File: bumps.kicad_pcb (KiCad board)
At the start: 2 copper layers, 111.1 x 65.4 mm, 126 parts, among them M1 CONN_1, M2 CONN_1, M3 CONN_1, P1 Micro-E, P10 Mot-A, P11 Mot-A, P12 Mot-X, P13 T1, P14 T2, P15 T3, P16 MPower, P17 PWM-2, P18 PWM-1, P19 END-X, P2 DIL6, P20 END-Y, P21 END-Z, P22 Mot-X, P23 Mot-Y, P24 Mot-Y, P25 Mot-Z, P26 Mot-Z, P27 Aux, P29 PWM, P3 Mot-E, P4 Mot-E, P5 DIL6, P6 DIL6, P7 DIL6, P8 P8 Header, P9 P9 Header, Q1 N-FET, Q2 N-FET, Q3 FDS9926A, Q4 FDS9926A, U1 E-Polo, U2 A-Polo, U3 X-Polo, U4 Y-Polo, U5 Z-Polo, U6 MC34063, U7 AP1117/3.3

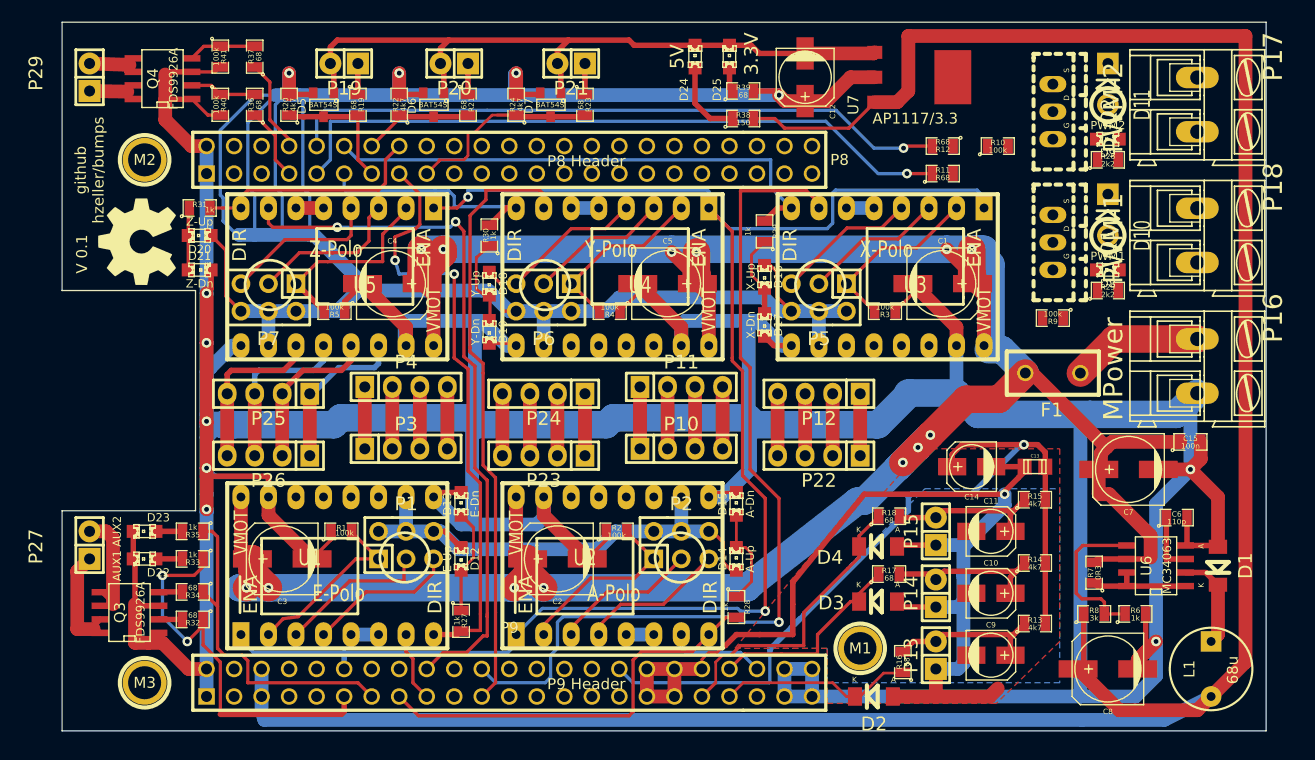
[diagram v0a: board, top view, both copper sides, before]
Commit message: o Solve 3.3V connect between two areas.
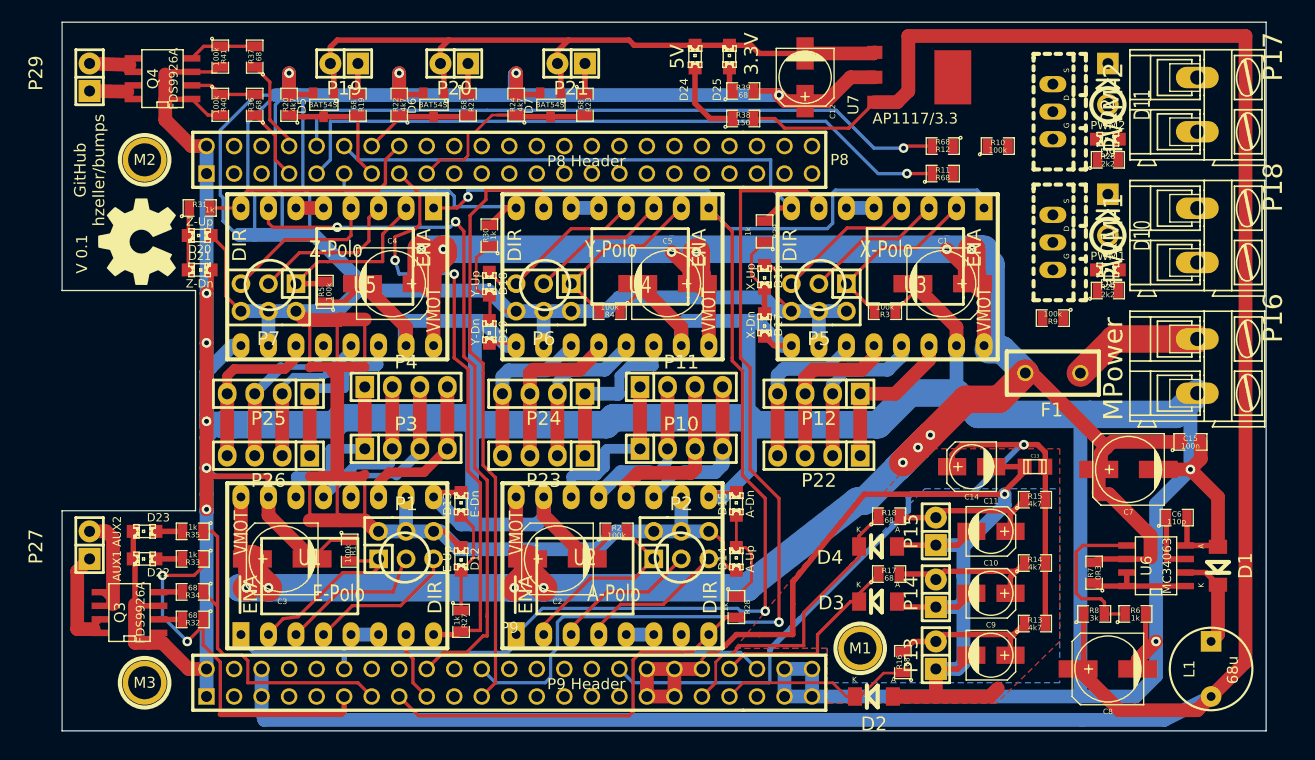
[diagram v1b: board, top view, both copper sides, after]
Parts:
- moved R5 1.99 mm to (71.9, 52.8), turned to 90 degrees
- moved R1 1.93 mm to (74.2, 76.7), turned to 270 degrees
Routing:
- net VDD_3V3: track 283.2 -> 347.6 mm
- net AGND: track 103.3 -> 114.8 mm
- net Net-(P3-Pad1): track 5.72 -> 16.2 mm
- net Net-(P23-Pad1): track 5.71 -> 15.9 mm
- net Net-(P10-Pad1): track 5.72 -> 15.9 mm
- net Net-(P12-Pad2): track 5.71 -> 15.8 mm
- net Net-(P10-Pad3): track 5.72 -> 15.6 mm
- net Net-(P12-Pad3): track 5.71 -> 15.4 mm
- net Net-(P23-Pad3): track 5.71 -> 15.3 mm
- net Net-(P12-Pad4): track 5.71 -> 15.2 mm
- net Net-(P10-Pad4): track 5.72 -> 14.9 mm
- net Net-(P23-Pad4): track 5.71 -> 14.8 mm
- net Net-(P3-Pad2): track 5.72 -> 14.8 mm
- net Net-(P10-Pad2): track 5.72 -> 14.8 mm
- net Net-(P23-Pad2): track 5.71 -> 14.7 mm
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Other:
- board text added: "GitHub hzeller/bumps"
- board text removed: "github hzeller/bumps"

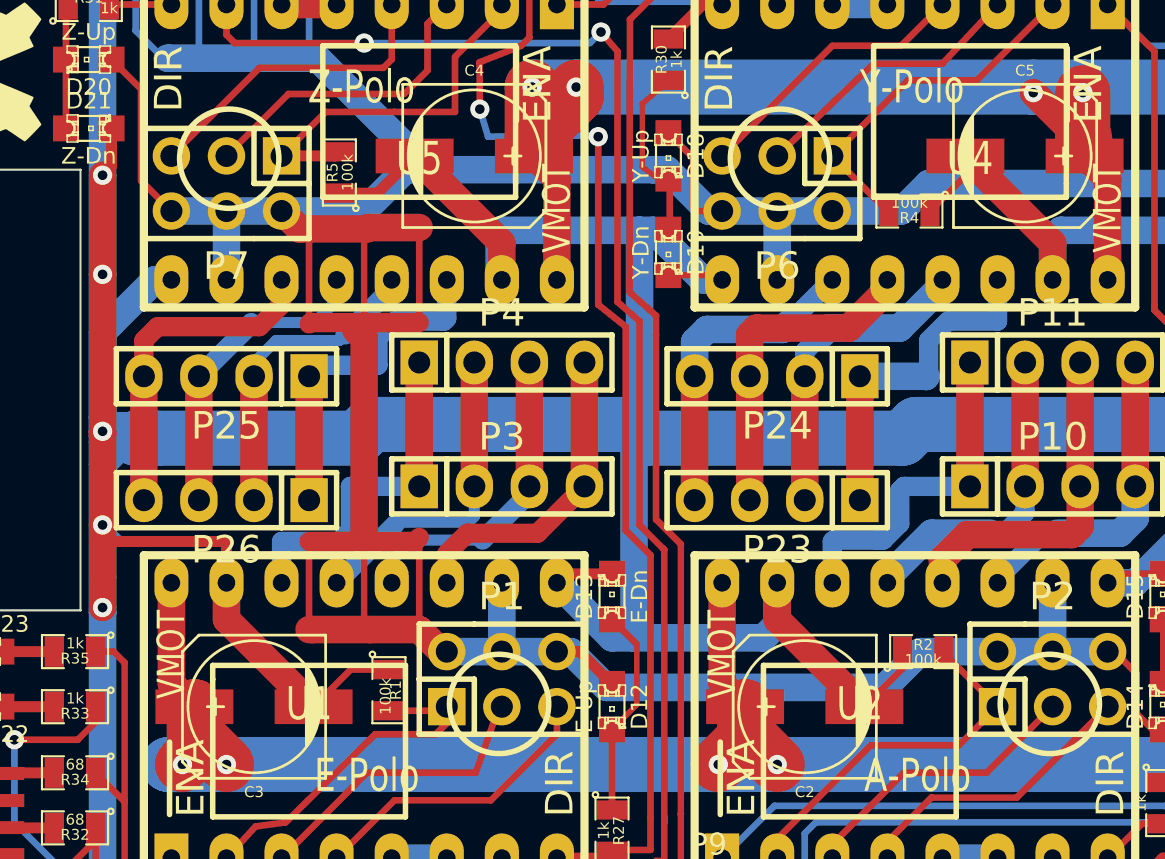
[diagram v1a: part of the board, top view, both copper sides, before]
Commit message: o A bit more symmetrical 3.3V solution.
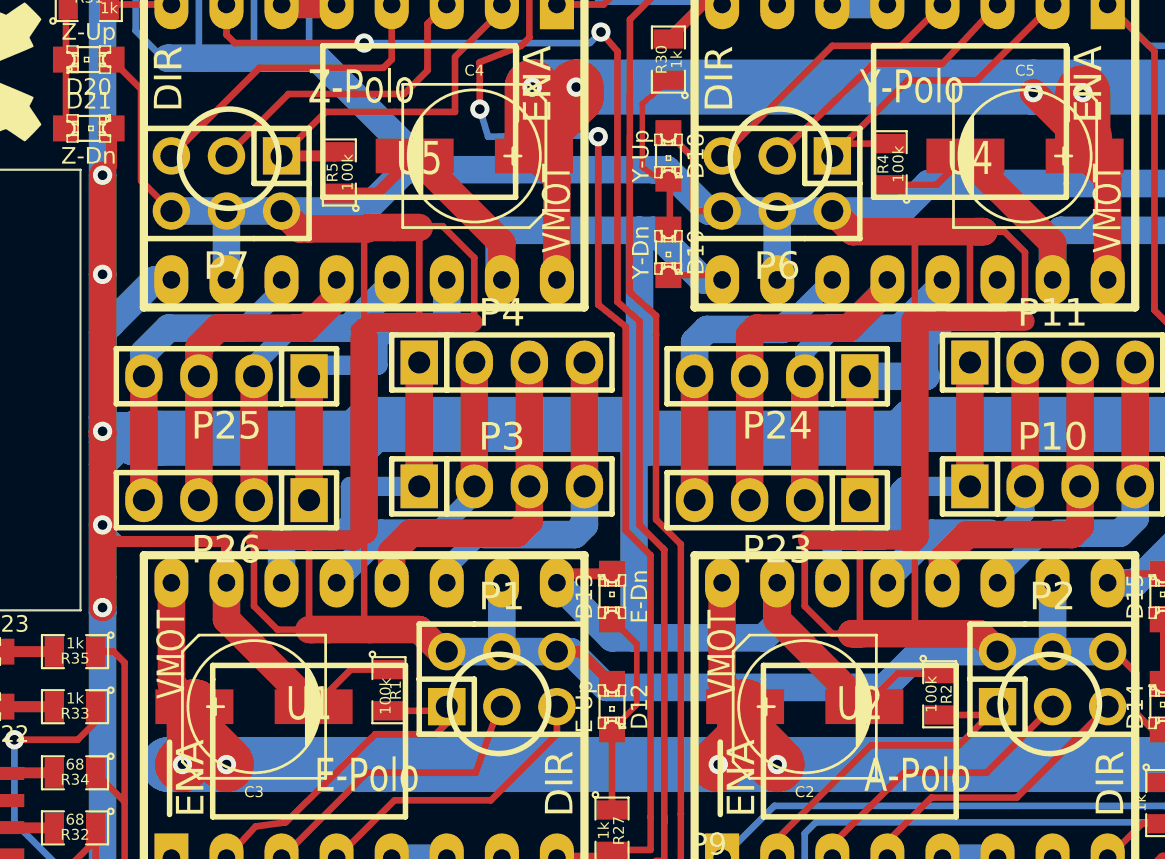
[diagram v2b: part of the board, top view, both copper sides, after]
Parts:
- moved R4 2.33 mm to (97.3, 52.5), turned to 90 degrees
- moved R2 2.11 mm to (99.6, 76.9), turned to 270 degrees
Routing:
- net VDD_3V3: track 347.6 -> 416.7 mm
- net GND: track 581.4 -> 583.9 mm
- net Net-(P3-Pad3): track 14.7 -> 16.0 mm
- net Net-(P6-Pad1): track 16.7 -> 16.0 mm
- net Net-(P25-Pad4): track 15.5 -> 14.8 mm
- net Net-(P2-Pad1): track 17.1 -> 16.4 mm
- net Net-(P25-Pad3): track 14.5 -> 15.2 mm
- net Net-(P3-Pad4): track 14.7 -> 15.4 mm

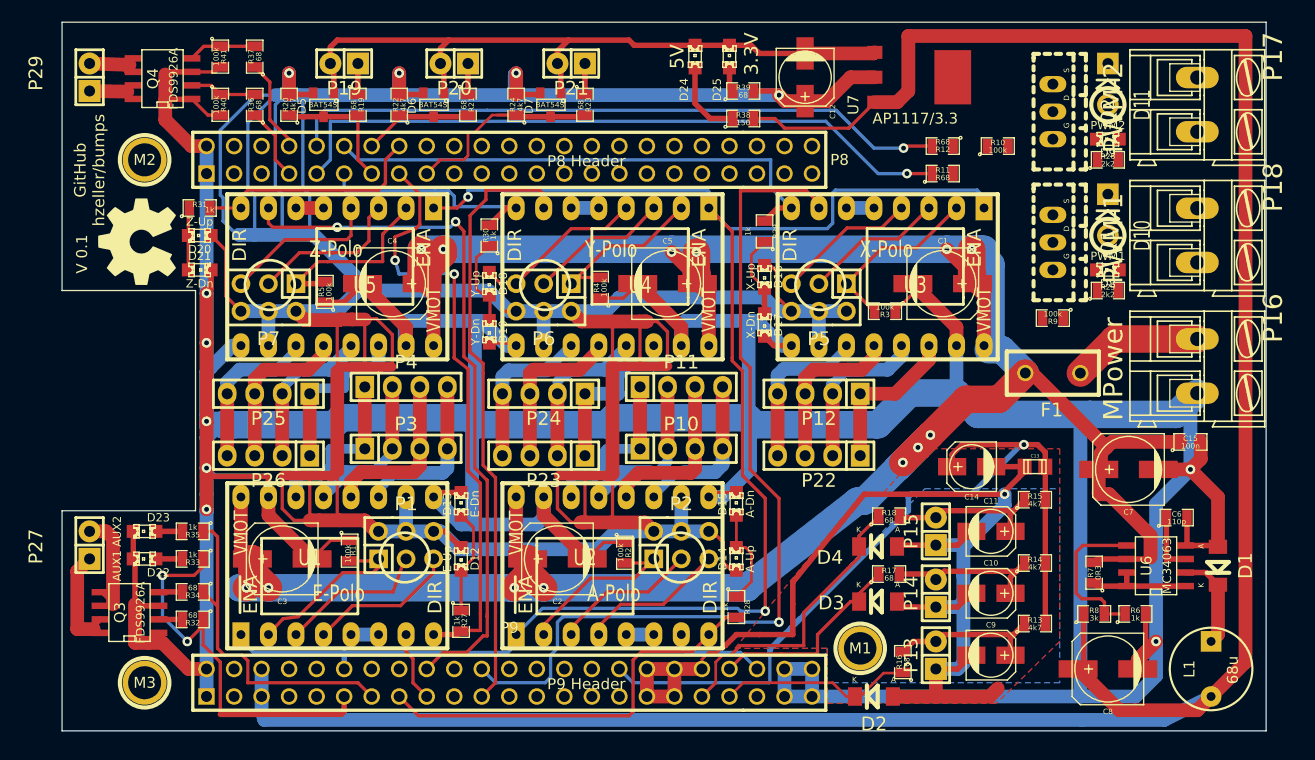
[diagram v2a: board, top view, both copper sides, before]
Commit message: o connect power PWM o start GND plane.
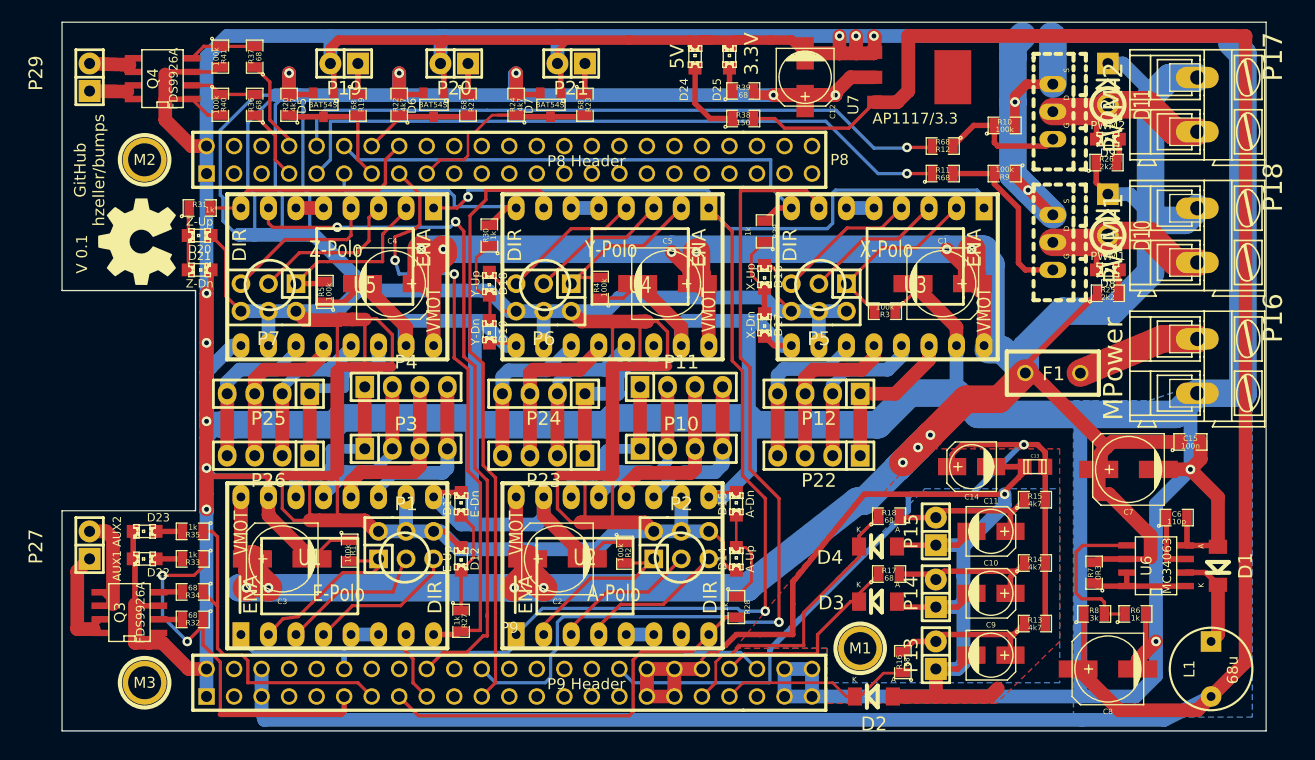
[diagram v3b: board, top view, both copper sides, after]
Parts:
- moved R9 14.1 mm to (134.6, 41.9)
- moved R10 2.01 mm to (134.6, 37.5)
- moved R26 0.28 mm to (144.0, 40.9)
- moved R25 0.25 mm to (144.1, 53.0)
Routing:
- net GND: track 583.9 -> 809.0 mm, vias 7 -> 12
- net VMOT: track 255.7 -> 322.8 mm
- net Net-(D10-Pad1): track 0.00 -> 18.2 mm
- net Net-(D11-Pad1): track 0.00 -> 18.2 mm
- net Net-(Q1-PadG): track 0.00 -> 16.4 mm
- net Net-(Q2-PadG): track 0.00 -> 12.0 mm
- net VDD_3V3: track 416.7 -> 425.0 mm, vias 4 -> 5
- net Net-(D8-Pad1): track 0.00 -> 2.52 mm
- net Net-(D9-Pad1): track 0.00 -> 2.25 mm
- net Net-(F1-Pad1): track 12.1 -> 11.4 mm
- added copper zone on B.Cu, net GND

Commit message: o more GND planes.
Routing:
- added copper zone on F.Cu, net GND
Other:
- board text added: "Stop X"
- board text added: "Stop Y"
- board text added: "Stop Z"
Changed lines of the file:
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@@
     (area 42.961076 19.039999 162.316583 94.234)
     (thickness 1.6)
-    (drawings 21)
+    (drawings 24)
     (tracks 1313)
     (zones 0)
@@
     (descr "1 pin")
     (tags "CONN DEV")
-    (fp_text reference P25 (at 0 -2.286 180) (layer F.SilkS)
+    (fp_text reference P25 (at 4.445 2.54 180) (layer F.SilkS)
       (effects (font (size 1.27 1.27) (thickness 0.2032)))
     )
@@
     (descr "1 pin")
     (tags "CONN DEV")
-    (fp_text reference P26 (at 0 -2.286 180) (layer F.SilkS)
+    (fp_text reference P26 (at 4.445 -1.905 180) (layer F.SilkS)
       (effects (font (size 1.27 1.27) (thickness 0.2032)))
     )
@@
     (descr "1 pin")
     (tags "CONN DEV")
-    (fp_text reference P3 (at 0 -2.286) (layer F.SilkS)
+    (fp_text reference P3 (at 3.81 1.905) (layer F.SilkS)
       (effects (font (size 1.27 1.27) (thickness 0.2032)))
     )
@@
     (descr "1 pin")
     (tags "CONN DEV")
-    (fp_text reference P4 (at 0 -2.286) (layer F.SilkS)
+    (fp_text reference P4 (at 5.08 -1.905) (layer F.SilkS)
       (effects (font (size 1.27 1.27) (thickness 0.2032)))
     )
@@
       (xy -2.42316 3.59156)) (layer F.SilkS) (width 0.00254))
   )
+  (gr_text "Stop Z" (at 94.615 29.21) (layer F.SilkS)
+    (effects (font (size 1.0668 1.0668) (thickness 0.2032)))
+  )
+  (gr_text "Stop Y" (at 83.82 29.21) (layer F.SilkS)
+    (effects (font (size 1.0668 1.0668) (thickness 0.2032)))
+  )
+  (gr_text "Stop X" (at 73.66 29.21) (layer F.SilkS)
+    (effects (font (size 1.0668 1.0668) (thickness 0.2032)))
+  )
   (gr_text "V 0.1" (at 49.4665 49.3395 90) (layer F.SilkS)
     (effects (font (size 1.016 1.016) (thickness 0.254)))
@@
     (polygon
       (pts
-        (xy 157.48 92.075) (xy 140.97 92.075) (xy 140.97 62.865) (xy 147.955 62.865) (xy 151.765 61.595)
-        (xy 157.48 61.595)
+        (xy 157.48 92.075) (xy 140.97 92.075) (xy 140.97 67.31) (xy 134.62 67.31) (xy 134.62 43.18)
+        (xy 60.96 43.18) (xy 60.96 52.07) (xy 48.26 52.07) (xy 48.26 29.21) (xy 157.48 29.21)
+        (xy 157.48 61.595) (xy 157.48 67.31) (xy 157.48 92.075)
+      )
+    )
+  )
+  (zone (net 15) (net_name GND) (layer F.Cu) (hatch edge 0.508)
+    (connect_pads (clearance 0.508))
+    (min_thickness 0.254)
+    (fill (arc_segments 16) (thermal_gap 0.508) (thermal_bridge_width 0.508))
+    (polygon
+      (pts
+        (xy 157.48 92.71) (xy 140.97 92.71) (xy 140.97 66.04) (xy 134.62 66.04) (xy 134.62 43.18)
+        (xy 118.11 43.18) (xy 118.11 38.1) (xy 60.96 38.1) (xy 60.96 52.07) (xy 48.26 52.07)
+        (xy 48.26 29.21) (xy 134.62 29.21) (xy 135.89 29.21) (xy 157.48 29.21) (xy 157.48 92.71)
+      )
+    )
+  )
+  (zone (net 15) (net_name GND) (layer F.Cu) (hatch edge 0.508)
+    (connect_pads (clearance 0.508))
+    (min_thickness 0.254)
+    (fill (arc_segments 16) (thermal_gap 0.508) (thermal_bridge_width 0.508))
+    (polygon
+      (pts
+        (xy 62.23 92.71) (xy 48.26 92.71) (xy 48.26 73.66) (xy 62.23 73.66)
+      )
+    )
+  )
+  (zone (net 15) (net_name GND) (layer B.Cu) (hatch edge 0.508)
+    (connect_pads (clearance 0.508))
+    (min_thickness 0.254)
+    (fill (arc_segments 16) (thermal_gap 0.508) (thermal_bridge_width 0.508))
+    (polygon
+      (pts
+        (xy 48.26 73.66) (xy 62.23 73.66) (xy 62.23 92.71) (xy 48.26 92.71)
       )
     )
